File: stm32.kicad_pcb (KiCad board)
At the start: 4 copper layers, 50 x 100 mm, 163 parts, among them CN1 SM04B-SRSS-TB (LF)(SN), CN2 SM04B-SRSS-TB (LF)(SN), CN3 SM04B-SRSS-TB (LF)(SN), J1 PZ254V-11-03P_C2937625, J2 PZ254V-11-03P_C2937625, J3 B2B-PH-SM4-TB (LF)(SN), J5 PZ254V-11-03P_C2937625, P1 TYPE-C 16PIN 2MD(073), Q1 DMG2301L-7, SW1 JS102011JCQN, SW2 6.0*6.0*6.0, SW3 6.0*6.0*6.0, U1 STM32L431KBU6_C2826408, U10 MAX3221ECPWR, U11 HB-PH9-12727PB2GOB, U12 TMP75AIDR, U13 CH340C_C7464026, U2 MCP73833T-AMI/MF, U3 TPS631000DRLR, U4 OPT3004DNPR, U5 XC6206P332MR_C347376, U6 INA260AIPWR, U8 MPU6500, U9 SN74AHCT1G125DBVR, X1 SC-32S32.768kHz20PPM7pF

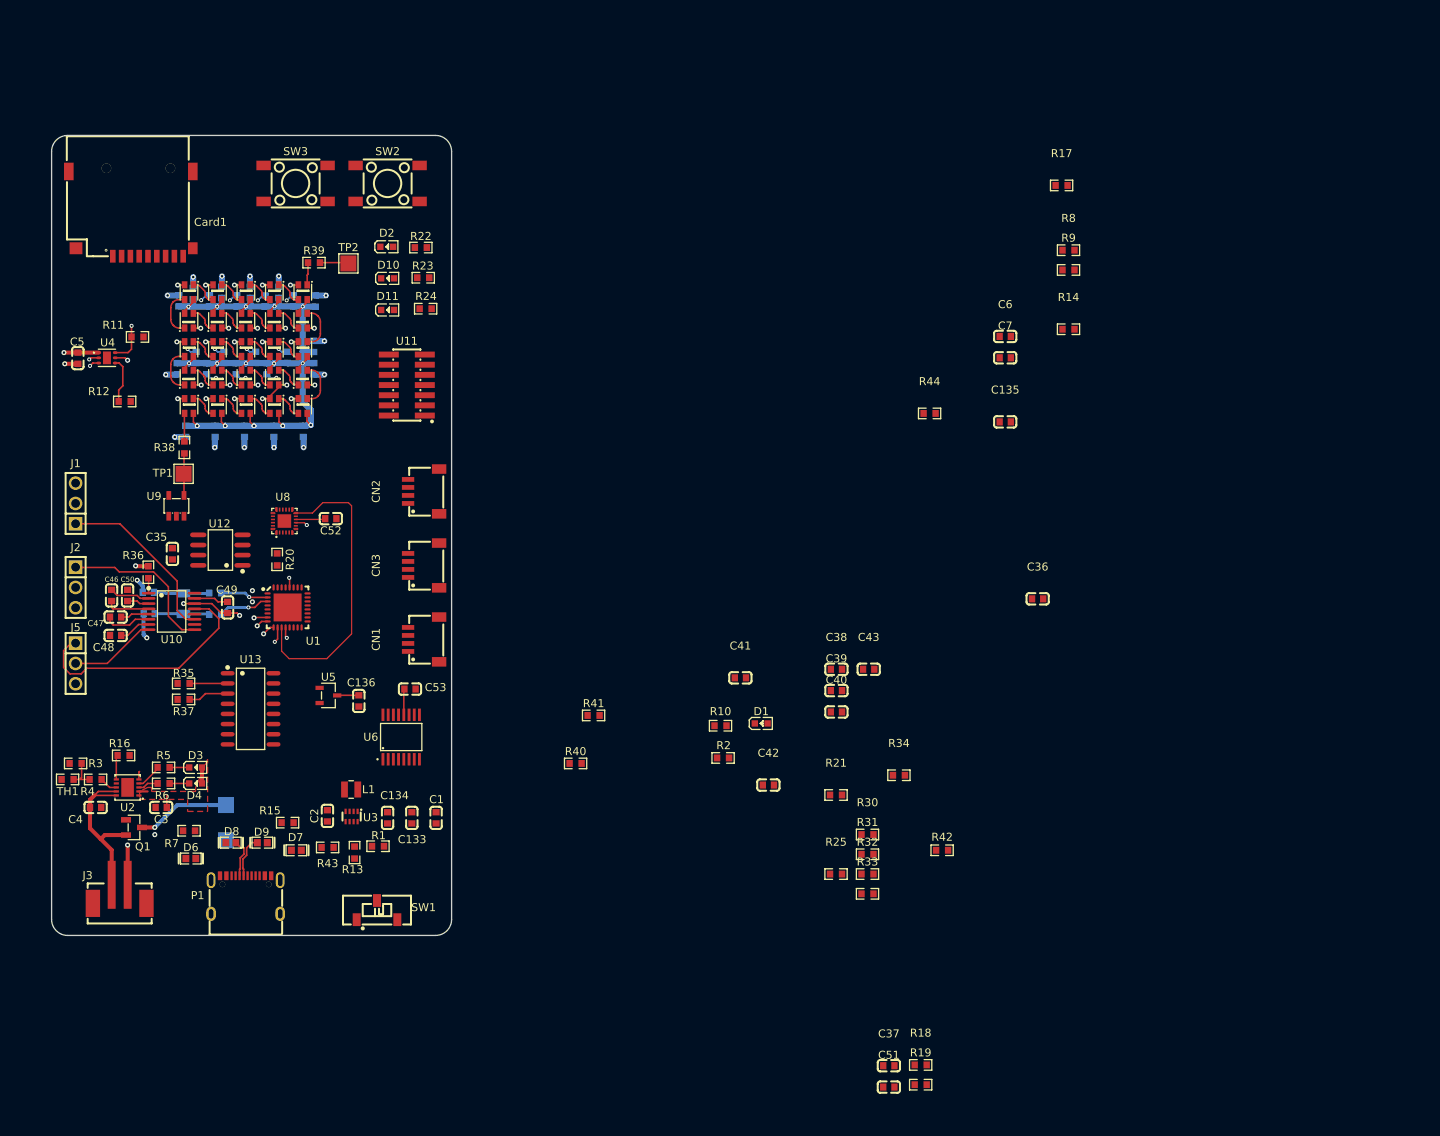
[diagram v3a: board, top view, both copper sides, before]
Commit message: Finished placement , added few TP's
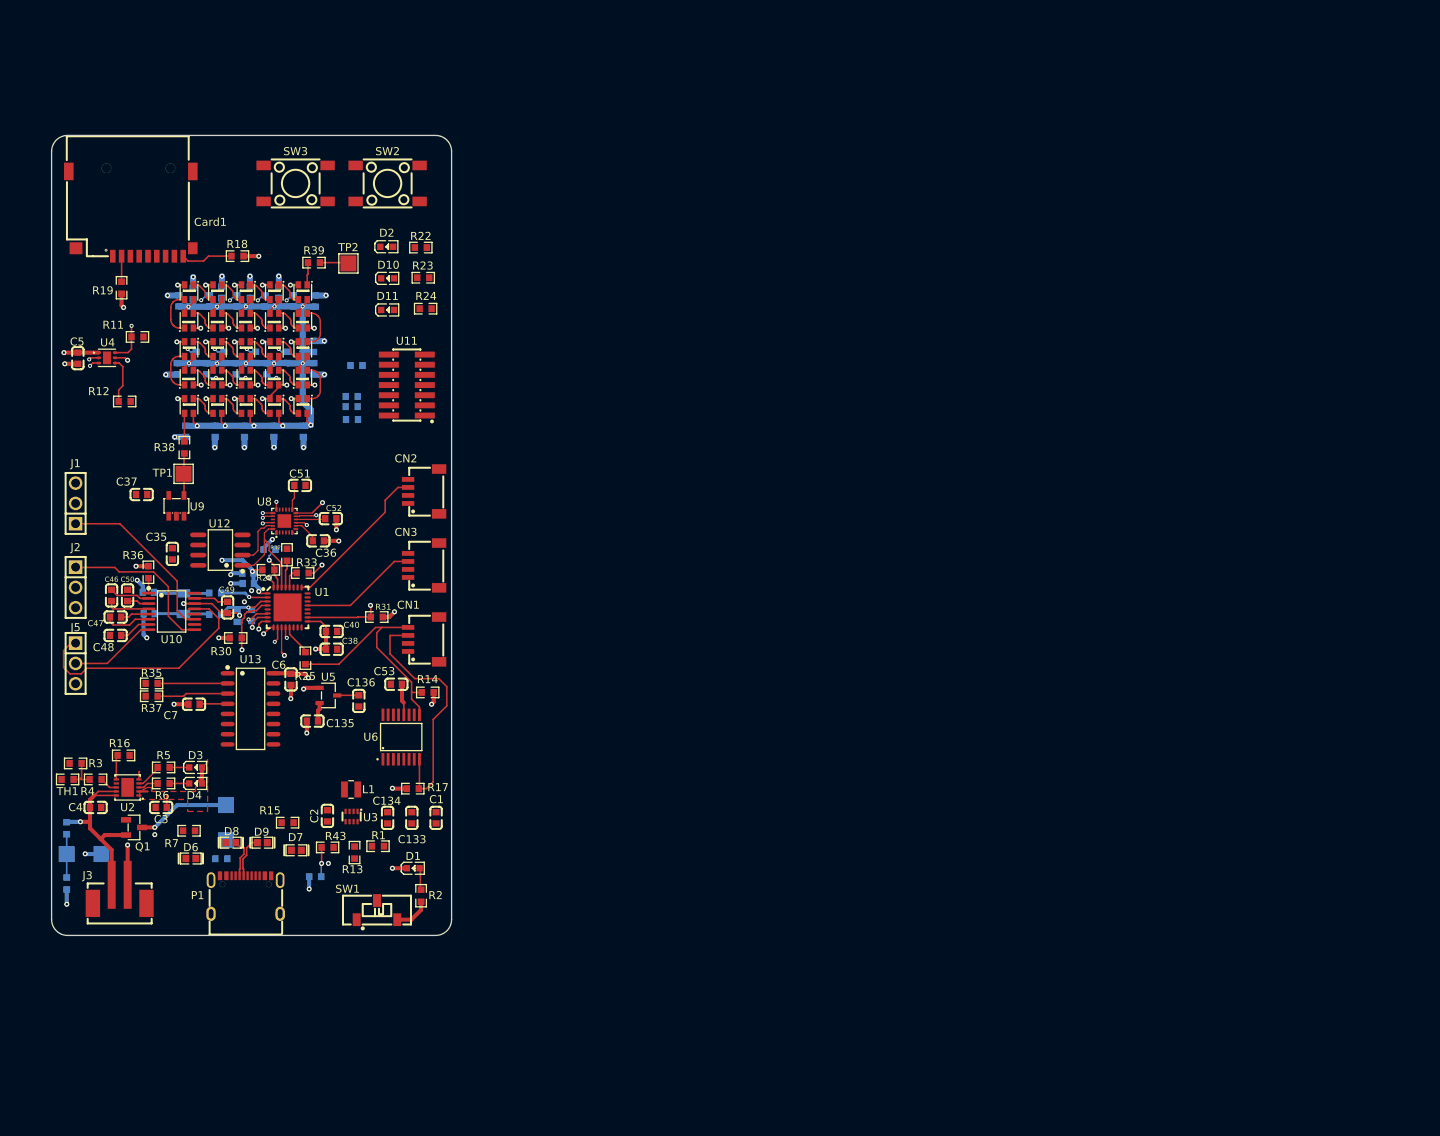
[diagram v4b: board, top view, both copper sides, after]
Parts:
- added +: TestPoint, TestPoint:TestPoint_Pad_2.0x2.0mm, B.Cu at (51.4, 123.8)
- added -: TestPoint, TestPoint:TestPoint_Pad_2.0x2.0mm, B.Cu at (55.7, 123.8)
- C39, C41, C42, C43, R10, R21, R34, R40, R41, R42, R44, R8, R9: moved to B.Cu
- moved R9 146.9 mm to (51.4, 127.5), turned to 90 degrees
- moved R8 144.6 mm to (51.4, 120.6), turned to 90 degrees
- moved R19 141.1 mm to (58.2, 53.0), turned to -90 degrees
- moved R18 132.3 mm to (72.7, 49.1)
- moved C37 117.6 mm to (60.8, 78.9)
- moved R17 110.7 mm to (94.7, 115.7), turned to 180 degrees
- moved C7 110.3 mm to (67.3, 105.1)
- moved C51 105.2 mm to (80.5, 77.7), turned to 180 degrees
- moved C6 99.0 mm to (79.4, 102.0), turned to 90 degrees
- moved R44 96.2 mm to (82.5, 126.7)
- moved R42 95.0 mm to (87.6, 62.8), turned to 180 degrees
- moved C135 94.3 mm to (82.1, 107.2)
- moved R14 92.1 mm to (96.5, 103.6)
- moved C36 90.2 mm to (82.8, 84.7), turned to 180 degrees
- moved R34 83.2 mm to (87.0, 66.6)
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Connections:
- C10 pad 1: /stm32_page/UART2_RX -> GND
- C11 pad 1: /stm32_page/UART2_RX -> GND
- C12 pad 1: /stm32_page/UART2_RX -> GND
- C13 pad 1: /stm32_page/UART2_RX -> GND
- C14 pad 1: /stm32_page/UART2_RX -> GND
- C15 pad 1: /stm32_page/UART2_RX -> GND
- C16 pad 1: /stm32_page/UART2_RX -> GND
- C17 pad 1: /stm32_page/UART2_RX -> GND
- C18 pad 1: /stm32_page/UART2_RX -> GND
- C19 pad 1: /stm32_page/UART2_RX -> GND
- C20 pad 1: /stm32_page/UART2_RX -> GND
- C21 pad 1: /stm32_page/UART2_RX -> GND
- C22 pad 1: /stm32_page/UART2_RX -> GND
- C23 pad 1: /stm32_page/UART2_RX -> GND
- C24 pad 1: /stm32_page/UART2_RX -> GND
- C25 pad 1: /stm32_page/UART2_RX -> GND
- C26 pad 1: /stm32_page/UART2_RX -> GND
- C27 pad 1: /stm32_page/UART2_RX -> GND
- C28 pad 1: /stm32_page/UART2_RX -> GND
- C29 pad 1: /stm32_page/UART2_RX -> GND
- C30 pad 1: /stm32_page/UART2_RX -> GND
- C31 pad 1: /stm32_page/UART2_RX -> GND
- C32 pad 1: /stm32_page/UART2_RX -> GND
- C33 pad 1: /stm32_page/UART2_RX -> GND
- C34 pad 1: /stm32_page/UART2_RX -> GND
- C44 pad 1: /stm32_page/UART2_RX -> GND
- C45 pad 1: /stm32_page/UART2_RX -> GND
- C49 pad 1: /stm32_page/UART2_RX -> GND
- J3 pad 1: /stm32_page/UART2_RX -> GND
- J5 pad 3: /stm32_page/UART2_RX -> GND
- LED10 pad 2: /stm32_page/UART2_RX -> GND
- LED11 pad 2: /stm32_page/UART2_RX -> GND
- LED12 pad 2: /stm32_page/UART2_RX -> GND
- LED13 pad 2: /stm32_page/UART2_RX -> GND
- LED14 pad 2: /stm32_page/UART2_RX -> GND
- LED15 pad 2: /stm32_page/UART2_RX -> GND
- LED16 pad 2: /stm32_page/UART2_RX -> GND
- LED17 pad 2: /stm32_page/UART2_RX -> GND
- LED18 pad 2: /stm32_page/UART2_RX -> GND
- LED19 pad 2: /stm32_page/UART2_RX -> GND
- LED2 pad 2: /stm32_page/UART2_RX -> GND
- LED20 pad 2: /stm32_page/UART2_RX -> GND
- LED21 pad 2: /stm32_page/UART2_RX -> GND
- LED22 pad 2: /stm32_page/UART2_RX -> GND
- LED23 pad 2: /stm32_page/UART2_RX -> GND
- LED24 pad 2: /stm32_page/UART2_RX -> GND
- LED25 pad 2: /stm32_page/UART2_RX -> GND
- LED26 pad 2: /stm32_page/UART2_RX -> GND
- LED3 pad 2: /stm32_page/UART2_RX -> GND
- LED4 pad 2: /stm32_page/UART2_RX -> GND
- LED5 pad 2: /stm32_page/UART2_RX -> GND
- LED6 pad 2: /stm32_page/UART2_RX -> GND
- LED7 pad 2: /stm32_page/UART2_RX -> GND
- LED8 pad 2: /stm32_page/UART2_RX -> GND
- LED9 pad 2: /stm32_page/UART2_RX -> GND
- P1 pad 13: /stm32_page/UART2_RX -> GND
- P1 pad 14: /stm32_page/UART2_RX -> GND
- R33 pad 1: /stm32_page/RGB_LEDS -> /stm32_page/RGB_LEDS_R
- R36 pad 2: /stm32_page/UART2_RX -> GND
- U1 pad 10: /stm32_page/UART2_RX -> /stm32_page/SD_CD
- U1 pad 28: /stm32_page/RGB_LEDS -> /stm32_page/RGB_LEDS_R
- U10 pad 14: /stm32_page/UART2_RX -> GND
- U8 pad 9: /stm32_page/UART2_RX -> GND
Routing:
- net GND: track 5.19 -> 113.0 mm, vias 3 -> 81
- net /stm32_page/UART2_RX: track 81.4 -> 1.58 mm, vias 62 -> 2
- net +3V3: track 8.66 -> 45.5 mm, vias 1 -> 12
- net /stm32_page/I2C3_SDA: track 0.00 -> 31.8 mm
- net /stm32_page/IMU_INT: track 37.1 -> 7.52 mm, vias 0 -> 2
- net /stm32_page/I2C3_SCL: track 0.00 -> 29.4 mm
- net /stm32_page/PWM_CH1: track 0.00 -> 19.4 mm
- net /stm32_page/PWM_CH4: track 0.00 -> 14.8 mm
- net /sensors/SDA: track 5.70 -> 19.9 mm
- net /stm32_page/PB_SW1: track 0.00 -> 9.39 mm, vias 0 -> 1
- net /stm32_page/SD_CD: track 0.00 -> 8.48 mm, vias 0 -> 1
- net /stm32_page/STM32_NRST: track 0.00 -> 7.93 mm, vias 0 -> 1
- net /sensors/SCL: track 5.14 -> 11.9 mm
- net /stm32_page/BOOT0: track 0.00 -> 5.51 mm, vias 0 -> 1
- net Net-(R8-Pad1): track 0.00 -> 5.40 mm
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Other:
- board text added: "Batt Volt/2"

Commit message: WIP routing still not finished
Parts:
- removed +, -: TestPoint, TestPoint:TestPoint_Pad_2.0x2.0mm
- added C54: CC0603KRX7R9BB104, easyeda2kicad:C0603, F.Cu at (95.8, 103.0)
- added TP3: TestPoint, TestPoint:TestPoint_Pad_2.0x2.0mm, F.Cu at (46.7, 122.7)
- added TP4: TestPoint, TestPoint:TestPoint_Pad_2.0x2.0mm, F.Cu at (46.7, 126.7)
- moved R14 9.78 mm to (90.2, 96.2), turned to 180 degrees
- moved R10 4.72 mm to (66.7, 126.9)
- moved R17 2.87 mm to (97.5, 115.0), turned to 0 degrees
- moved C53 1.08 mm to (93.6, 103.0), turned to 90 degrees
- moved D9 0.42 mm to (75.4, 122.4)
- turned R43 to 180 degrees
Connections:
- C1 pad 2: +5V -> /USB/5V_B4_INA
- C133 pad 2: +5V -> /USB/5V_B4_INA
- C134 pad 2: +5V -> /USB/5V_B4_INA
- C136 pad 2: Net-(U5-VIN) -> +5V
- C53 pad 1: +5V -> /USB/5V_B4_INA
- R1 pad 2: +5V -> /USB/5V_B4_INA
- U3 pad 1: +5V -> /USB/5V_B4_INA
- U5 pad 3: Net-(U5-VIN) -> +5V
- U6 pad 1: +5V -> /USB/5V_B4_INA
- U6 pad 10: +5V -> /USB/5V_B4_INA
- U6 pad 12: +5V -> /USB/5V_B4_INA
- U6 pad 14: Net-(U5-VIN) -> +5V
- U6 pad 15: Net-(U5-VIN) -> +5V
- U6 pad 16: Net-(U5-VIN) -> +5V
- U6 pad 2: +5V -> /USB/5V_B4_INA
- U6 pad 3: +5V -> /USB/5V_B4_INA
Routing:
- net +3V3: track 45.5 -> 386.2 mm, vias 12 -> 28
- net +5V: track 106.6 -> 254.2 mm, vias 15 -> 20
- net /stm32_page/VCP_RX: track 0.00 -> 114.7 mm, vias 0 -> 1
- net /stm32_page/VCP_TX: track 0.00 -> 84.1 mm, vias 0 -> 1
- net GND: track 113.0 -> 194.3 mm, vias 81 -> 166
- net +5VP: track 9.23 -> 80.3 mm, vias 1 -> 10
- net /stm32_page/UART2_RX: track 1.58 -> 64.5 mm, vias 2 -> 3
- net /USB/5V_B4_INA: track 0.00 -> 49.3 mm
- net /stm32_page/UART2_TX: track 1.84 -> 47.7 mm
- net /stm32_page/I2C3_SDA: track 31.8 -> 76.2 mm, vias 0 -> 2
- net /sensors/SCL: track 11.9 -> 54.2 mm, vias 1 -> 2
- net /USB/TXD_0: track 0.00 -> 39.8 mm, vias 0 -> 2
- net /sensors/SDA: track 19.9 -> 55.6 mm, vias 0 -> 2
- net /USB/raw_voltage: track 11.7 -> 42.7 mm, vias 1 -> 2
- net /USB/VIN: track 4.71 -> 34.6 mm, vias 0 -> 1
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- added copper zone on F.Cu, net +5V
- added copper zone on B.Cu, net +5VP
- added copper zone on F.Cu, net /USB/5V_B4_INA
- added copper zone on F.Cu, net GND

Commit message: Finished routing
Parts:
- +: renamed from TP3; moved to B.Cu
- -: renamed from TP4; moved to B.Cu
- moved - 10.0 mm to (56.4, 124.1), turned to 180 degrees
- moved + 4.92 mm to (51.4, 124.1), turned to 180 degrees
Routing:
- net /stm32_page/SPI1_MOSI: track 6.86 -> 100.8 mm, vias 1 -> 2
- net /stm32_page/PB_SW1: track 10.0 -> 103.8 mm, vias 1 -> 2
- net /stm32_page/STM32_NRST: track 8.05 -> 100.0 mm, vias 1 -> 2
- net /stm32_page/LED2: track 3.45 -> 66.6 mm, vias 1 -> 2
- net /stm32_page/LED1: track 6.42 -> 65.5 mm, vias 1 -> 2
- net /stm32_page/SPI1_MISO: track 1.36 -> 58.8 mm, vias 1 -> 2
- net /stm32_page/SPI1_SCK: track 3.19 -> 56.9 mm, vias 1 -> 2
- net /stm32_page/SD_CD: track 8.48 -> 61.7 mm, vias 1 -> 2
- net /stm32_page/SYS_WKUP1: track 7.44 -> 57.3 mm
- net +3V3: track 386.2 -> 430.8 mm, vias 28 -> 27
- net /stm32_page/LED3: track 1.99 -> 43.1 mm, vias 1 -> 2
- net /stm32_page/IMU_INT: track 7.52 -> 46.6 mm
- net /stm32_page/UART2_RX: track 64.5 -> 28.6 mm, vias 3 -> 1
- net /stm32_page/SWCLK: track 7.92 -> 38.6 mm, vias 2 -> 3
- net /stm32_page/RGB_LEDS: track 2.08 -> 32.0 mm, vias 1 -> 2
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
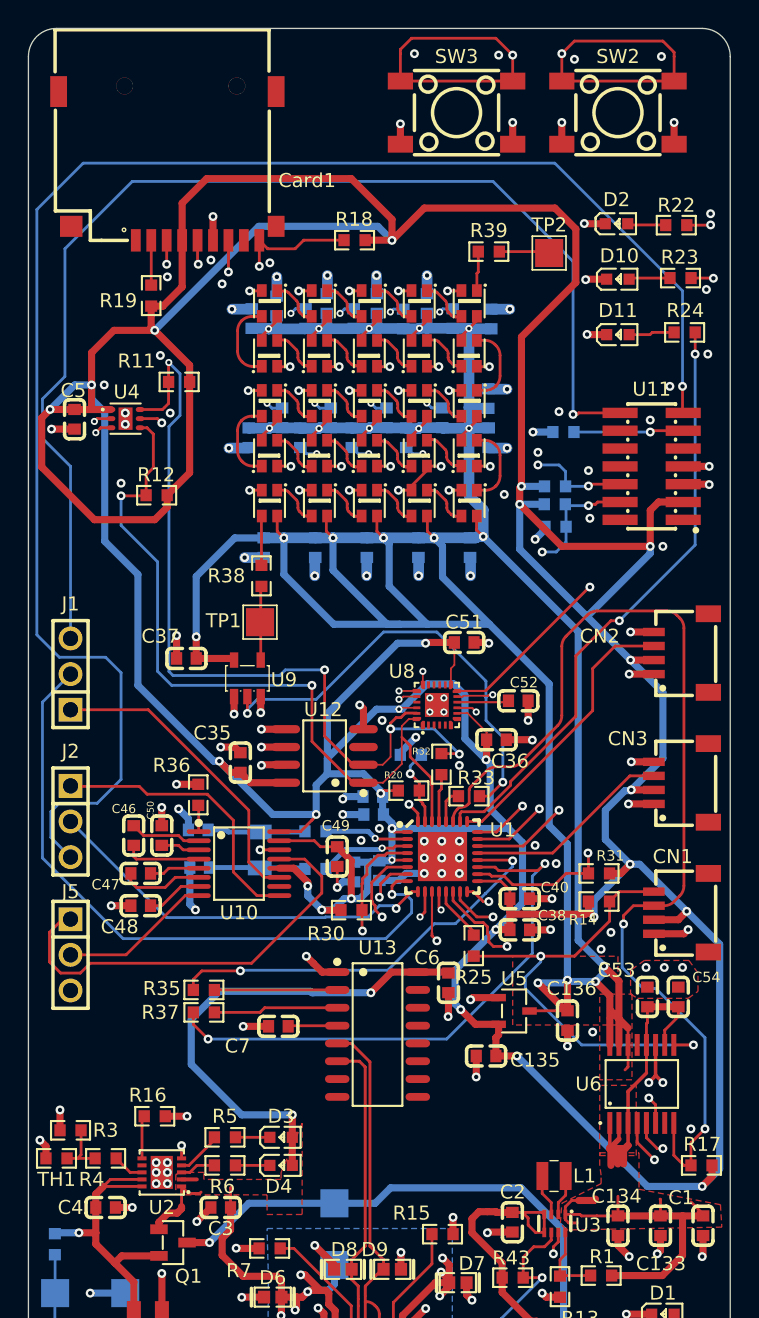
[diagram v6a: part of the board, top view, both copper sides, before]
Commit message: Swap L4 with L3 and finished routing
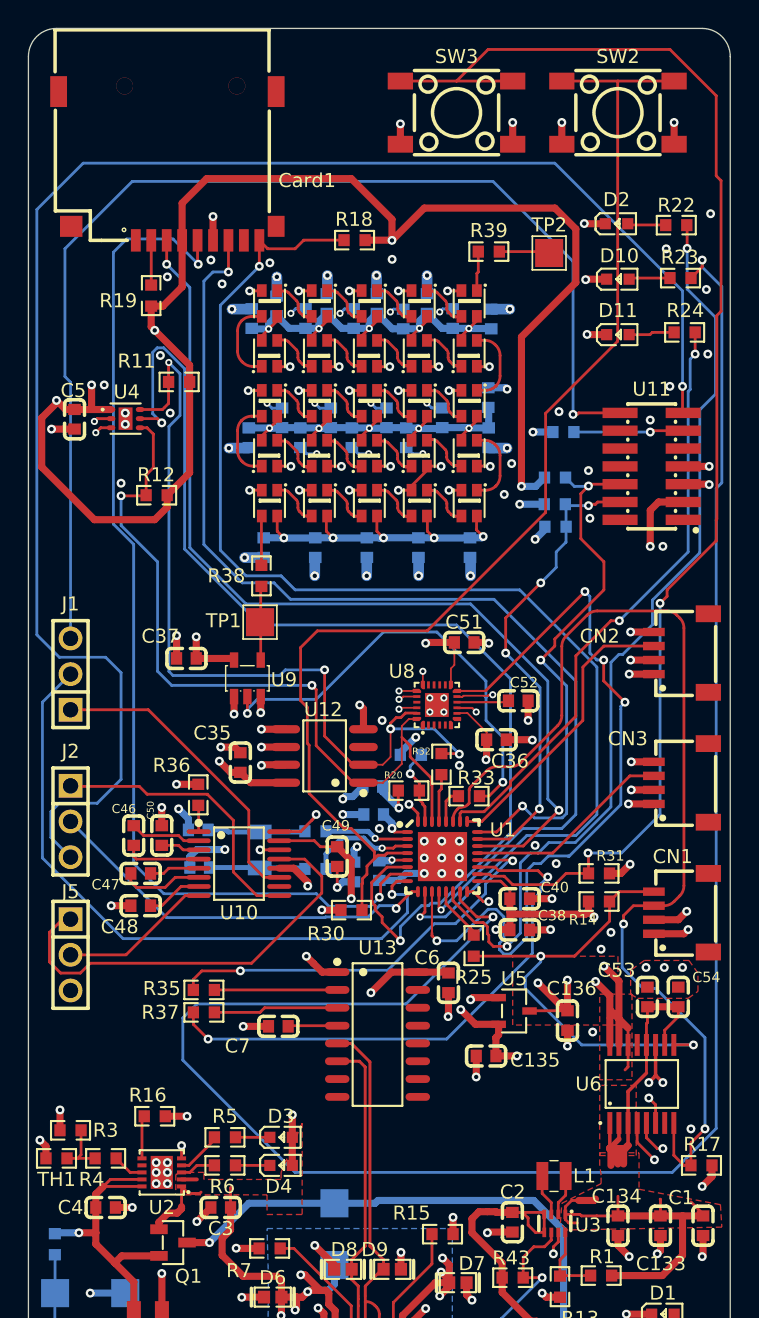
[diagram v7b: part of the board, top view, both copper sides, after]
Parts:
- moved C43 0.72 mm to (74.0, 88.0)
- moved R34 0.62 mm to (87.0, 66.0)
- moved C24 0.07 mm to (82.3, 60.3)
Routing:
- net /stm32_page/LED2: track 66.6 -> 138.4 mm
- net /stm32_page/SPI1_MOSI: track 100.8 -> 68.8 mm
- net +3V3: track 430.8 -> 404.0 mm, vias 27 -> 28
- net /stm32_page/SD_CD: track 61.7 -> 88.1 mm
- net +5V: track 254.2 -> 277.4 mm
- net /stm32_page/SYS_WKUP1: track 57.3 -> 80.5 mm
- net /stm32_page/SPI1_SCK: track 56.9 -> 75.3 mm
- net /stm32_page/SPI1_MISO: track 58.8 -> 77.2 mm
- net +5VP: track 77.9 -> 95.9 mm
- net /stm32_page/STM32_NRST: track 100.0 -> 86.4 mm, vias 2 -> 0
- net /stm32_page/IMU_INT: track 46.6 -> 56.9 mm, vias 2 -> 4
- net /stm32_page/PB_SW1: track 103.8 -> 98.3 mm
- net /stm32_page/SWDIO: track 32.4 -> 33.9 mm, vias 3 -> 4
- net /stm32_page/VCP_TX: track 84.1 -> 82.8 mm
- net Net-(U1-PC15-OSC32_OUT): track 6.48 -> 7.71 mm
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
